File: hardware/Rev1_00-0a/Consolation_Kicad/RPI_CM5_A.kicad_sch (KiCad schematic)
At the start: 58 parts, among them J17 61300311121, J19 RPI_CMx_A, J7 2998TR, Q19 SSM3K56FS,LF, Q20 SSM3K56FS,LF, Q21 SSM3K56FS,LF, Q22 SSM3K56FS,LF, Q26 SSM3K56FS,LF, U19 SN74LVC1G125DBVR, U21 MCP7940NT-I/MS, Y2 32.768kHz

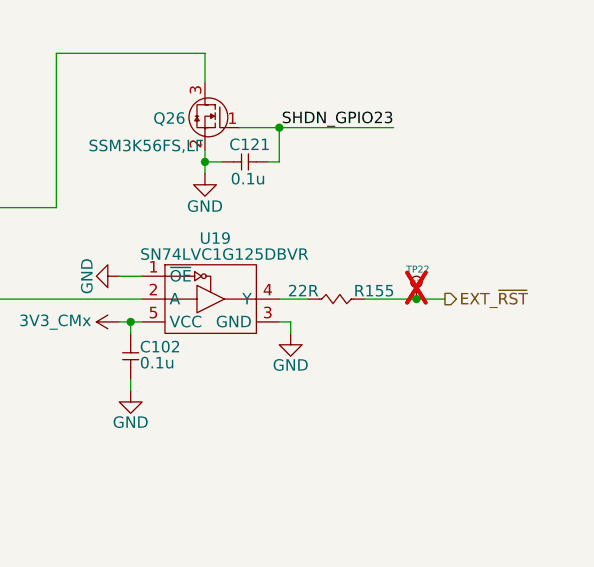
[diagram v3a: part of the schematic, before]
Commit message: Update ConJoy L2 trigger (2-level trigger instead) Update ConJoy all output files accordingly
Work on Consolation preliminary placement
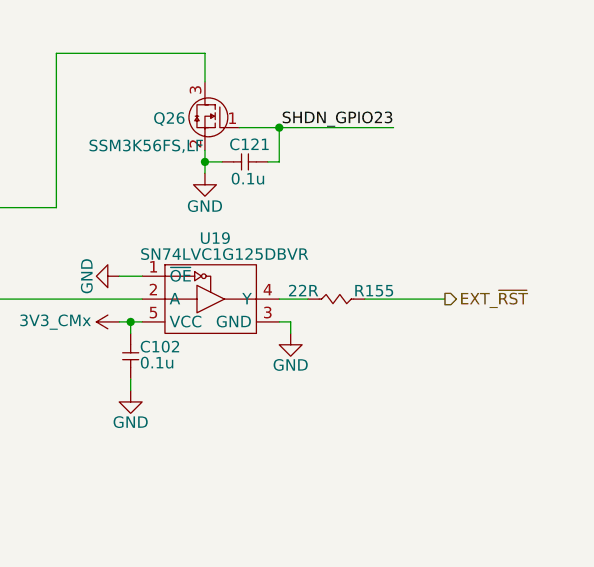
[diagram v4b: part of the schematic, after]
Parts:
- removed TP22: 28 mils, footprint:SMT_TP_28_MILS, symbol KicadCompDb:Test Point/TP_00001
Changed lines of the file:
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@@
 	(title_block
 		(title "Consolation [Console Emulation]")
-		(date "2026-08-08")
+		(date "2026-08-23")
 		(rev "1.00-0A")
 		(comment 1 "Jean-Francois Bilodeau")
@@
 	)
 	(junction
-		(at 271.145 141.605)
-		(diameter 0)
-		(color 0 0 0 0)
-	)
-	(junction
 		(at 49.53 161.925)
 		(diameter 0)
@@
 	(wire
 		(pts
-			(xy 271.145 141.605) (xy 274.32 141.605)
+			(xy 265.43 141.605) (xy 274.32 141.605)
 		)
 		(stroke
@@
 	(wire
 		(pts
-			(xy 265.43 141.605) (xy 271.145 141.605)
-		)
-		(stroke
-			(width 0)
-			(type default)
-		)
-	)
-	(wire
-		(pts
 			(xy 16.51 139.065) (xy 29.21 139.065)
 		)
@@
 					(unit 1)
 				)
-			)
-		)
-	)
-	(symbol
-		(lib_id "KicadCompDb:Test Point/TP_00001")
-		(at 271.145 140.335 90)
-		(unit 1)
-		(body_style 1)
-		(exclude_from_sim no)
-		(in_bom no)
-		(on_board yes)
-		(in_pos_files yes)
-		(dnp yes)
-		(property "Reference" "TP22"
-			(at 270.002 138.303 90)
-			(show_name no)
-			(do_not_autoplace no)
-			(effects
-				(font
-					(size 0.762 0.762)
-				)
-				(justify right)
-			)
-		)
-		(property "Value" "28 mils"
-			(at 272.161 139.7 0)
-			(hide yes)
-			(show_name no)
-			(do_not_autoplace no)
-			(effects
-				(font
-					(size 0.762 0.762)
-				)
-			)
-		)
-		(property "Footprint" "footprint:SMT_TP_28_MILS"
-			(at 273.05 140.335 0)
-			(hide yes)
-			(show_name no)
-			(do_not_autoplace no)
-			(effects
-				(font
-					(size 1.27 1.27)
-				)
-			)
-		)
-		(property "Datasheet" "NA"
-			(at 271.145 140.335 0)
-			(hide yes)
-			(show_name no)
-			(do_not_autoplace no)
-			(effects
-				(font
-					(size 1.27 1.27)
-				)
-			)
-		)
-		(property "Description" "SMT TP 28 mils"
-			(at 271.145 140.335 0)
-			(hide yes)
-			(show_name no)
-			(do_not_autoplace no)
-			(effects
-				(font
-					(size 1.27 1.27)
-				)
-			)
-		)
-		(property "Type" "SMT"
-			(at 271.145 140.335 0)
-			(hide yes)
-			(show_name yes)
-			(do_not_autoplace no)
-			(effects
-				(font
-					(size 1.27 1.27)
-				)
-			)
-		)
-		(property "Package" "NA"
-			(at 271.145 140.335 0)
-			(hide yes)
-			(show_name yes)
-			(do_not_autoplace no)
-			(effects
-				(font
-					(size 1.27 1.27)
-				)
-			)
-		)
-		(property "Operating Temperature" "NA"
-			(at 271.145 140.335 0)
-			(hide yes)
-			(show_name yes)
-			(do_not_autoplace no)
-			(effects
-				(font
-					(size 1.27 1.27)
-				)
-			)
-		)
-		(property "Dimensions" "28 mils"
-			(at 271.145 140.335 0)
-			(hide yes)
-			(show_name yes)
-			(do_not_autoplace no)
-			(effects
-				(font
-					(size 1.27 1.27)
-				)
-			)
-		)
-		(property "Manufacturer" "NA"
-			(at 271.145 140.335 0)
-			(hide yes)
-			(show_name yes)
-			(do_not_autoplace no)
-			(effects
-				(font
-					(size 1.27 1.27)
-				)
-			)
-		)
-		(property "Manufacturer Part Number" "NA"
-			(at 271.145 140.335 0)
-			(hide yes)
-			(show_name yes)
-			(do_not_autoplace no)
-			(effects
-				(font
-					(size 1.27 1.27)
-				)
-			)
-		)
-		(property "Distributor" "NA"
-			(at 271.145 140.335 0)
-			(hide yes)
-			(show_name yes)
-			(do_not_autoplace no)
-			(effects
-				(font
-					(size 1.27 1.27)
-				)
-			)
-		)
-		(property "Distributor Part Number" "NA"
-			(at 271.145 140.335 0)
-			(hide yes)
-			(show_name yes)
-			(do_not_autoplace no)
-			(effects
-				(font
-					(size 1.27 1.27)
-				)
-			)
-		)
-		(pin "1"
-		)
-		(instances
-			(project "Consolation_Kicad"
-				(path "/b18b5a64-cfe0-4447-acaf-556f3c6e6513/75d0c21e-3f51-4c04-91a3-13b7a2863fa1"
-					(reference "TP22")
-					(unit 1)
-				)

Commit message: Continue preliminary placement To do : Power supplies + Type C charger
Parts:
- R127, R83: now not fitted
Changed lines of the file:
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@@
 	(title_block
 		(title "Consolation [Console Emulation]")
-		(date "2026-08-23")
+		(date "2026-08-29")
 		(rev "1.00-0A")
 		(comment 1 "Jean-Francois Bilodeau")
@@
 		(on_board yes)
 		(in_pos_files yes)
-		(dnp no)
+		(dnp yes)
 		(property "Reference" "R127"
 			(at 150.241 175.26 90)
@@
 		(on_board yes)
 		(in_pos_files yes)
-		(dnp no)
+		(dnp yes)
 		(property "Reference" "R83"
 			(at 156.464 175.26 90)

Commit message: Preliminary routing
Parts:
- removed R151, R152: 0R, footprint:RES_0402, symbol KicadCompDb:Resistors/RES_SMT_00001
- added C124: 0.1u, footprint:CAP_NONPOL_0402, symbol KicadCompDb:Capacitors/CAP_CER_SMT_00001
- added Q27, Q28, Q29: SSM3K56FS,LF, footprint:SC-75, symbol KicadCompDb:Mosfet/MOSFET_00002
- added R136, R142: 10K, footprint:RES_0402, symbol KicadCompDb:Resistors/RES_SMT_00013
- added TP54, TP55: 75 mils, footprint:SMT_TP_75_MILS, symbol KicadCompDb:Test Point/TP_00004
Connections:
- net GPIO_VREF is gone; now on net 3V3_CMx: J19.78 (GPIO_VREF)
- net 5V0: now also R136.2, R142.2
- net GND: now also C124.1, Q27.2 (S), Q28.2 (S), Q29.2 (S)
- net ~{VOL_DOWN}: now also Q28.1 (G)
- net ~{VOL_UP}: now also Q27.1 (G)
- net ~{CM5_SHDN}: now reaches J19.92 (RUN_PG/PWR_BTN), Q26.3 (D)
- net ~{CM5_SHDN}: now also Q29.3 (D), R142.1, TP54.1
- new net HW_SHDN: C124.2, Q27.3 (D), Q28.3 (D), Q29.1 (G), R136.1, TP55.1
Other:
- moved on the sheet: C102, C121, Q26, R155, U19
